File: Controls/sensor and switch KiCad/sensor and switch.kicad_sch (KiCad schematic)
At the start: 16 parts, among them U12 Spark MAX Motor Controller, U16 Spark MAX Motor Controller, U2 Jetson Nano, U20 Spark MAX Motor Controller, U24 Rev Neo, U25 Rev Neo, U26 Rev Neo, U27 Rev Neo, U3 Rev Neo, U5 Spark MAX Motor Controller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

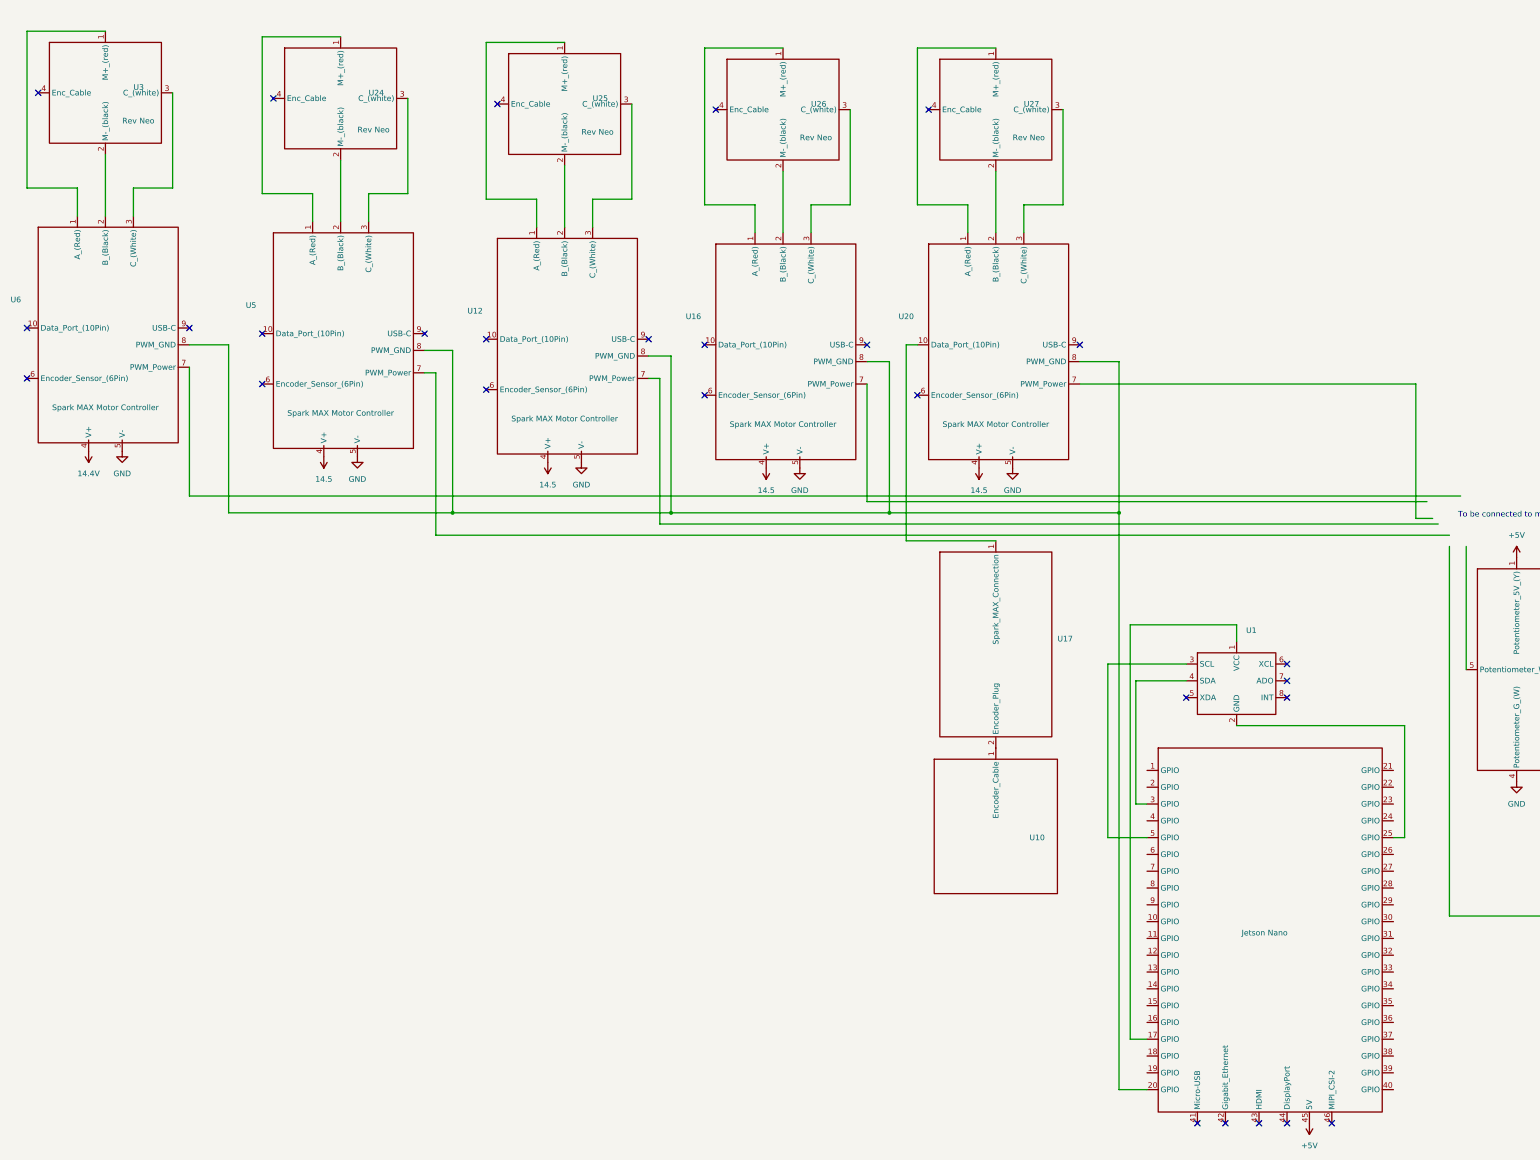
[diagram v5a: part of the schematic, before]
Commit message: Updated controls to match Overall Schematic
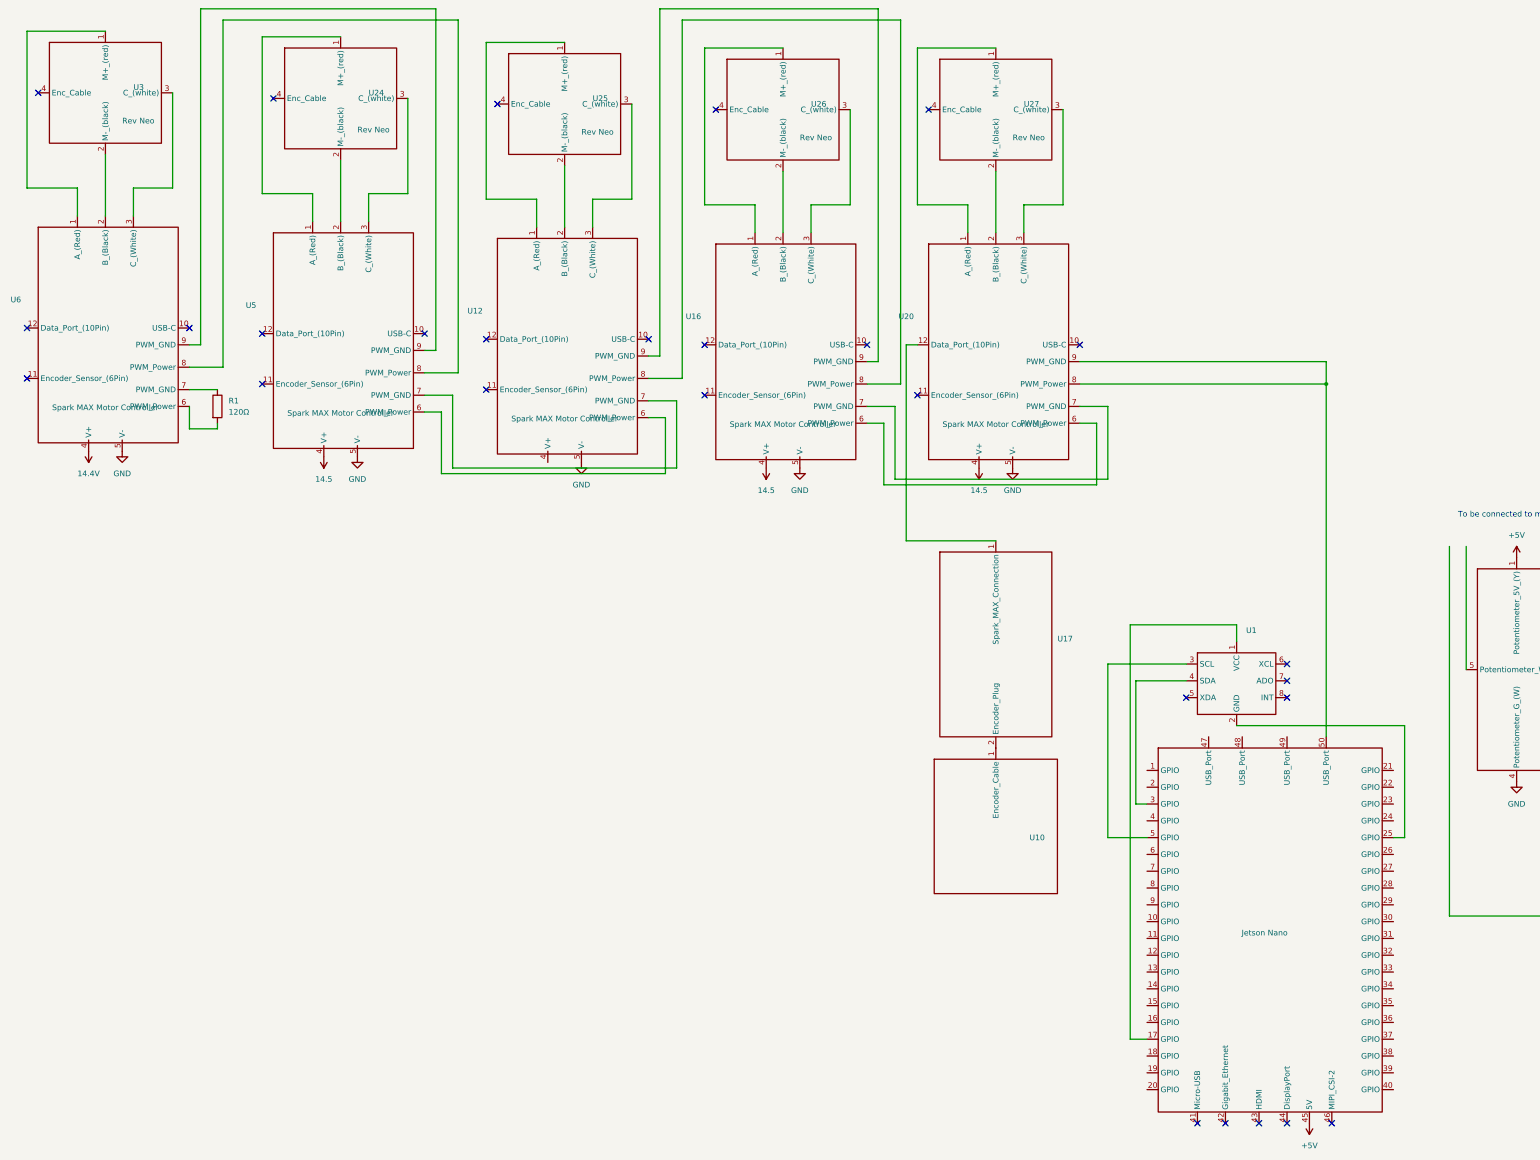
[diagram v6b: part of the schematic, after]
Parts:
- added R1: 120Ω, symbol Device:R
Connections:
- net 14.5: no longer U12.4 (V+)
- net at U17.1 (Spark_MAX_Connection): now also U20.12 (Data_Port_(10Pin)); no longer U20.10 (Data_Port_(10Pin))
- net at U12.6 (PWM_Power): now also U5.6 (PWM_Power)
- net at U12.7 (PWM_GND): now also U5.7 (PWM_GND)
- net at U12.9 (PWM_GND): now also U16.9 (PWM_GND)
- net at U6.6 (PWM_Power): now also R1.2
- net at U6.7 (PWM_GND): now also R1.1
- net at U6.9 (PWM_GND): now also U5.9 (PWM_GND)
- net at U20.6 (PWM_Power): now also U16.6 (PWM_Power)
- net at U20.7 (PWM_GND): now also U16.7 (PWM_GND)
- net at U20.9 (PWM_GND): now also U2.50 (USB_Port), U20.8 (PWM_Power)
- new net: U12.8 (PWM_Power), U16.8 (PWM_Power)
- new net: U5.8 (PWM_Power), U6.8 (PWM_Power)
- now unconnected: U2.20 (GPIO)

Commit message: Completed Update of Spark Max & Potentiometer Connections to Jetson Nano
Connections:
- net GND: no longer U29.8 (PWM_GND)
- net at U28.5 (Potentiometer_Wiper_(Blu)): now also U2.31 (GPIO)
- net at U29.6 (PWM_Power): now also U2.50 (USB_Port), U29.7 (PWM_GND)
- net at U29.9 (PWM_GND): now also U20.9 (PWM_GND)
- new net: U20.8 (PWM_Power), U29.8 (PWM_Power)
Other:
- note removed: "To be connected to microcontroller"
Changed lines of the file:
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@@
 	(generator_version "9.0")
 	(paper "A2")
-	(text "To be connected to microcontroller"
-		(exclude_from_sim no)
-		(at 488.442 165.608 0)
-		(effects
-			(font
-				(size 1.27 1.27)
-			)
-		)
-	)
 	(junction
-		(at 443.23 135.89)
+		(at 566.42 237.49)
 		(diameter 0)
 		(color 0 0 0 0)
@@
 	(wire
 		(pts
+			(xy 458.47 261.62) (xy 464.82 261.62)
+		)
+		(stroke
+			(width 0)
+			(type default)
+		)
+	)
+	(wire
+		(pts
 			(xy 289.56 139.7) (xy 295.91 139.7)
 		)
@@
 	(wire
 		(pts
+			(xy 566.42 255.27) (xy 468.63 255.27)
+		)
+		(stroke
+			(width 0)
+			(type default)
+		)
+	)
+	(wire
+		(pts
 			(xy 345.44 140.97) (xy 345.44 157.48)
 		)
@@
 	(wire
 		(pts
-			(xy 443.23 130.81) (xy 443.23 135.89)
-		)
-		(stroke
-			(width 0)
-			(type default)
-		)
-	)
-	(wire
-		(pts
 			(xy 374.65 101.6) (xy 374.65 95.25)
 		)
@@
 	(wire
 		(pts
+			(xy 464.82 261.62) (xy 464.82 200.66)
+		)
+		(stroke
+			(width 0)
+			(type default)
+		)
+	)
+	(wire
+		(pts
+			(xy 468.63 255.27) (xy 468.63 207.01)
+		)
+		(stroke
+			(width 0)
+			(type default)
+		)
+	)
+	(wire
+		(pts
+			(xy 568.96 135.89) (xy 568.96 228.6)
+		)
+		(stroke
+			(width 0)
+			(type default)
+		)
+	)
+	(wire
+		(pts
 			(xy 185.42 140.97) (xy 185.42 146.05)
 		)
@@
 	(wire
 		(pts
+			(xy 561.34 233.68) (xy 566.42 233.68)
+		)
+		(stroke
+			(width 0)
+			(type default)
+		)
+	)
+	(wire
+		(pts
 			(xy 302.26 95.25) (xy 302.26 59.69)
 		)
@@
 	(wire
 		(pts
+			(xy 561.34 223.52) (xy 565.15 223.52)
+		)
+		(stroke
+			(width 0)
+			(type default)
+		)
+	)
+	(wire
+		(pts
 			(xy 234.95 92.71) (xy 234.95 71.12)
 		)
@@
 	(wire
 		(pts
-			(xy 387.35 135.89) (xy 443.23 135.89)
+			(xy 387.35 135.89) (xy 568.96 135.89)
 		)
 		(stroke
@@
 	(wire
 		(pts
-			(xy 474.98 172.72) (xy 474.98 200.66)
-		)
-		(stroke
-			(width 0)
-			(type default)
-		)
-	)
-	(wire
-		(pts
 			(xy 238.76 133.35) (xy 246.38 133.35)
 		)
@@
 	(wire
 		(pts
+			(xy 443.23 207.01) (xy 443.23 215.9)
+		)
+		(stroke
+			(width 0)
+			(type default)
+		)
+	)
+	(wire
+		(pts
 			(xy 193.04 132.08) (xy 193.04 53.34)
 		)
@@
 	(wire
 		(pts
+			(xy 468.63 207.01) (xy 443.23 207.01)
+		)
+		(stroke
+			(width 0)
+			(type default)
+		)
+	)
+	(wire
+		(pts
 			(xy 313.69 95.25) (xy 302.26 95.25)
 		)
@@
 	(wire
 		(pts
-			(xy 561.34 256.54) (xy 561.34 228.6)
-		)
-		(stroke
-			(width 0)
-			(type default)
-		)
-	)
-	(wire
-		(pts
 			(xy 166.37 83.82) (xy 166.37 97.79)
 		)
@@
 	(wire
 		(pts
-			(xy 443.23 135.89) (xy 443.23 215.9)
+			(xy 561.34 237.49) (xy 566.42 237.49)
 		)
 		(stroke
@@
 	(wire
 		(pts
-			(xy 471.17 172.72) (xy 471.17 256.54)
-		)
-		(stroke
-			(width 0)
-			(type default)
-		)
-	)
-	(wire
-		(pts
 			(xy 341.63 50.8) (xy 341.63 130.81)
 		)
@@
 	(wire
 		(pts
-			(xy 471.17 256.54) (xy 561.34 256.54)
-		)
-		(stroke
-			(width 0)
-			(type default)
-		)
-	)
-	(wire
-		(pts
 			(xy 342.9 144.78) (xy 342.9 158.75)
 		)
@@
 	(wire
 		(pts
+			(xy 464.82 200.66) (xy 474.98 200.66)
+		)
+		(stroke
+			(width 0)
+			(type default)
+		)
+	)
+	(wire
+		(pts
 			(xy 285.75 93.98) (xy 285.75 72.39)
 		)
@@
 	(wire
 		(pts
+			(xy 387.35 130.81) (xy 565.15 130.81)
+		)
+		(stroke
+			(width 0)
+			(type default)
+		)
+	)
+	(wire
+		(pts
 			(xy 264.16 100.33) (xy 264.16 93.98)
 		)
@@
 	(wire
 		(pts
+			(xy 568.96 228.6) (xy 561.34 228.6)
+		)
+		(stroke
+			(width 0)
+			(type default)
+		)
+	)
+	(wire
+		(pts
 			(xy 201.93 92.71) (xy 201.93 57.15)
 		)
@@
 	(wire
 		(pts
+			(xy 565.15 223.52) (xy 565.15 130.81)
+		)
+		(stroke
+			(width 0)
+			(type default)
+		)
+	)
+	(wire
+		(pts
+			(xy 566.42 233.68) (xy 566.42 237.49)
+		)
+		(stroke
+			(width 0)
+			(type default)
+		)
+	)
+	(wire
+		(pts
 			(xy 347.98 171.45) (xy 368.3 171.45)
 		)
@@
 	(wire
 		(pts
-			(xy 387.35 130.81) (xy 443.23 130.81)
+			(xy 566.42 237.49) (xy 566.42 255.27)
 		)
 		(stroke
@@
 	(symbol
 		(lib_id "power:GND")
-		(at 561.34 223.52 90)
-		(unit 1)
-		(exclude_from_sim no)
-		(in_bom yes)
-		(on_board yes)
-		(dnp no)
-		(fields_autoplaced yes)
-		(property "Reference" "#PWR016"
-			(at 567.69 223.52 0)
-			(effects
-				(font
-					(size 1.27 1.27)
-				)
-				(hide yes)
-			)
-		)
-		(property "Value" "GND"
-			(at 565.15 223.5199 90)
-			(effects
-				(font
-					(size 1.27 1.27)
-				)
-				(justify right)
-			)
-		)
-		(property "Footprint" ""
-			(at 561.34 223.52 0)
-			(effects
-				(font
-					(size 1.27 1.27)
-				)
-				(hide yes)
-			)
-		)
-		(property "Datasheet" ""
-			(at 561.34 223.52 0)
-			(effects
-				(font
-					(size 1.27 1.27)
-				)
-				(hide yes)
-			)
-		)
-		(property "Description" "Power symbol creates a global label with name \"GND\" , ground"
-			(at 561.34 223.52 0)
-			(effects
-				(font
-					(size 1.27 1.27)
-				)
-				(hide yes)
-			)
-		)
-		(pin "1"
-		)
-		(instances
-			(project ""
-				(path "/11791a88-2599-4bc1-915b-e97e523e770e"
-					(reference "#PWR016")
-					(unit 1)
-				)
-			)
-		)
-	)
-	(symbol
-		(lib_id "power:GND")
 		(at 170.18 151.13 0)
 		(unit 1)
@@
 	)
 	(symbol
-		(lib_name "Spark_MAX_Motor_Controller_1")
 		(lib_id "Lunabotics 2025-26:Spark_MAX_Motor_Controller")
 		(at 542.29 226.06 0)
@@
 		(pin "5"
 		)
+		(pin "11"
+		)
+		(pin "12"
+		)
 		(instances
